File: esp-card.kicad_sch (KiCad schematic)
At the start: 15 parts, among them J1 Conn_01x01_Socket, J2 Conn_01x02_Socket, U1 XC6206P332MR, U2 ESP32-C3FH4, U3 TYPE_C-CQ-111PWB, U4 TS-1187A-B-A-B, U5 NH-B1010RGBT-HF, X1 CF4040M00015001

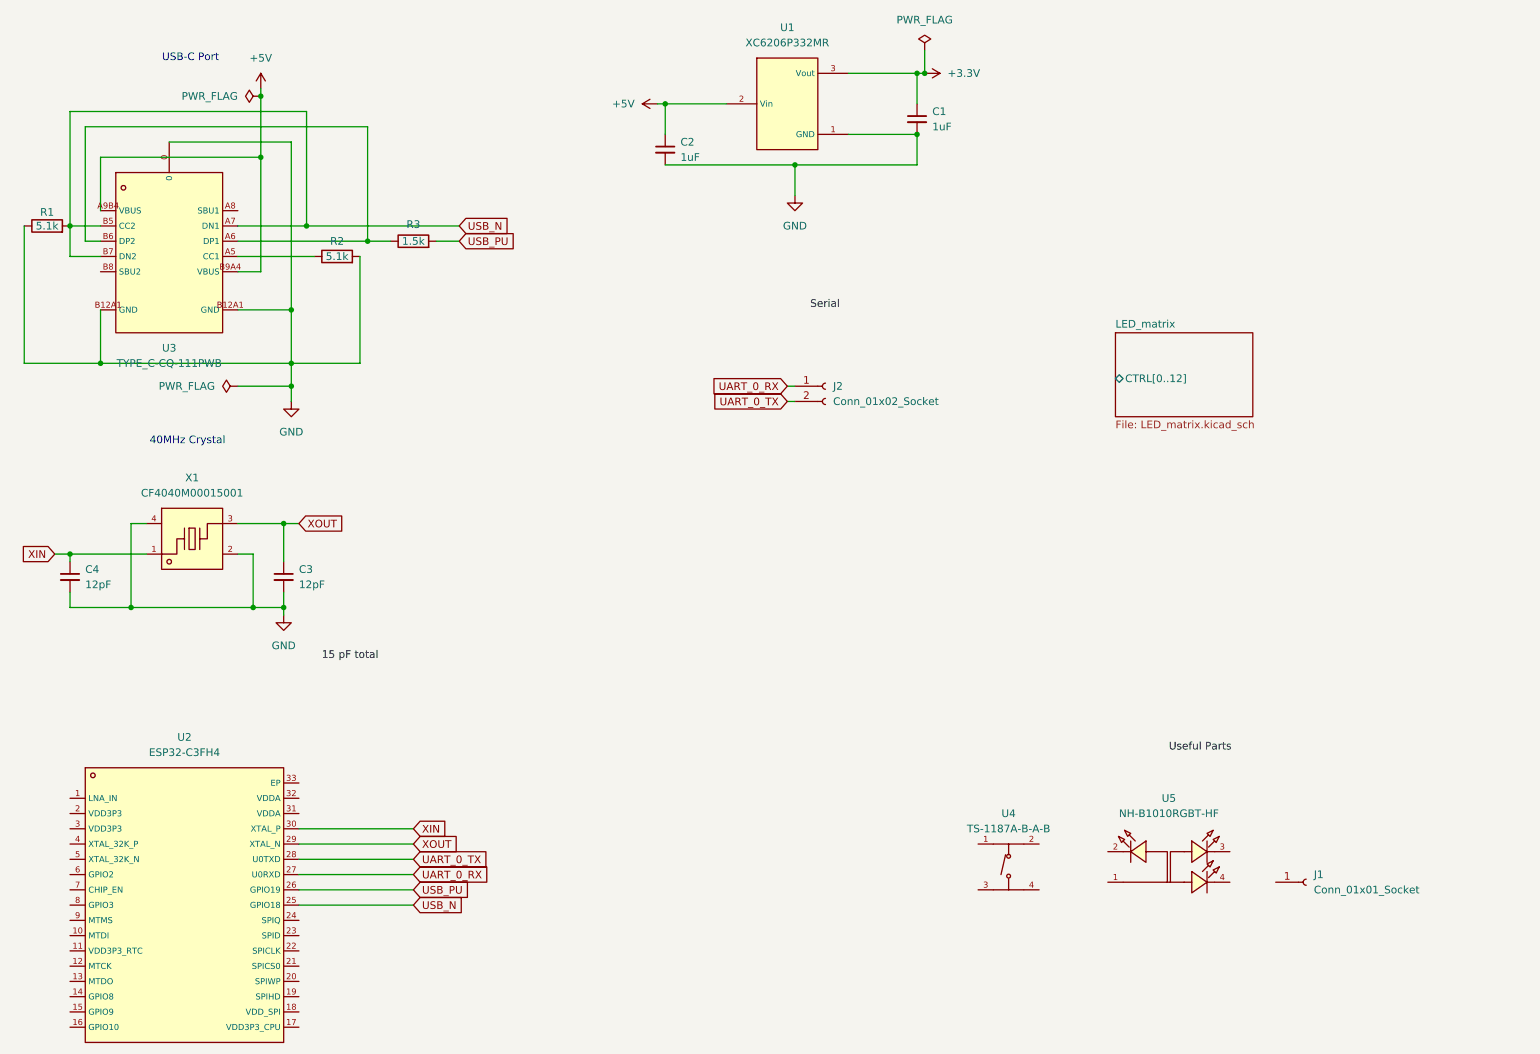
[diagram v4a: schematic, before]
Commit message: fix: corrected labels and hierarchy
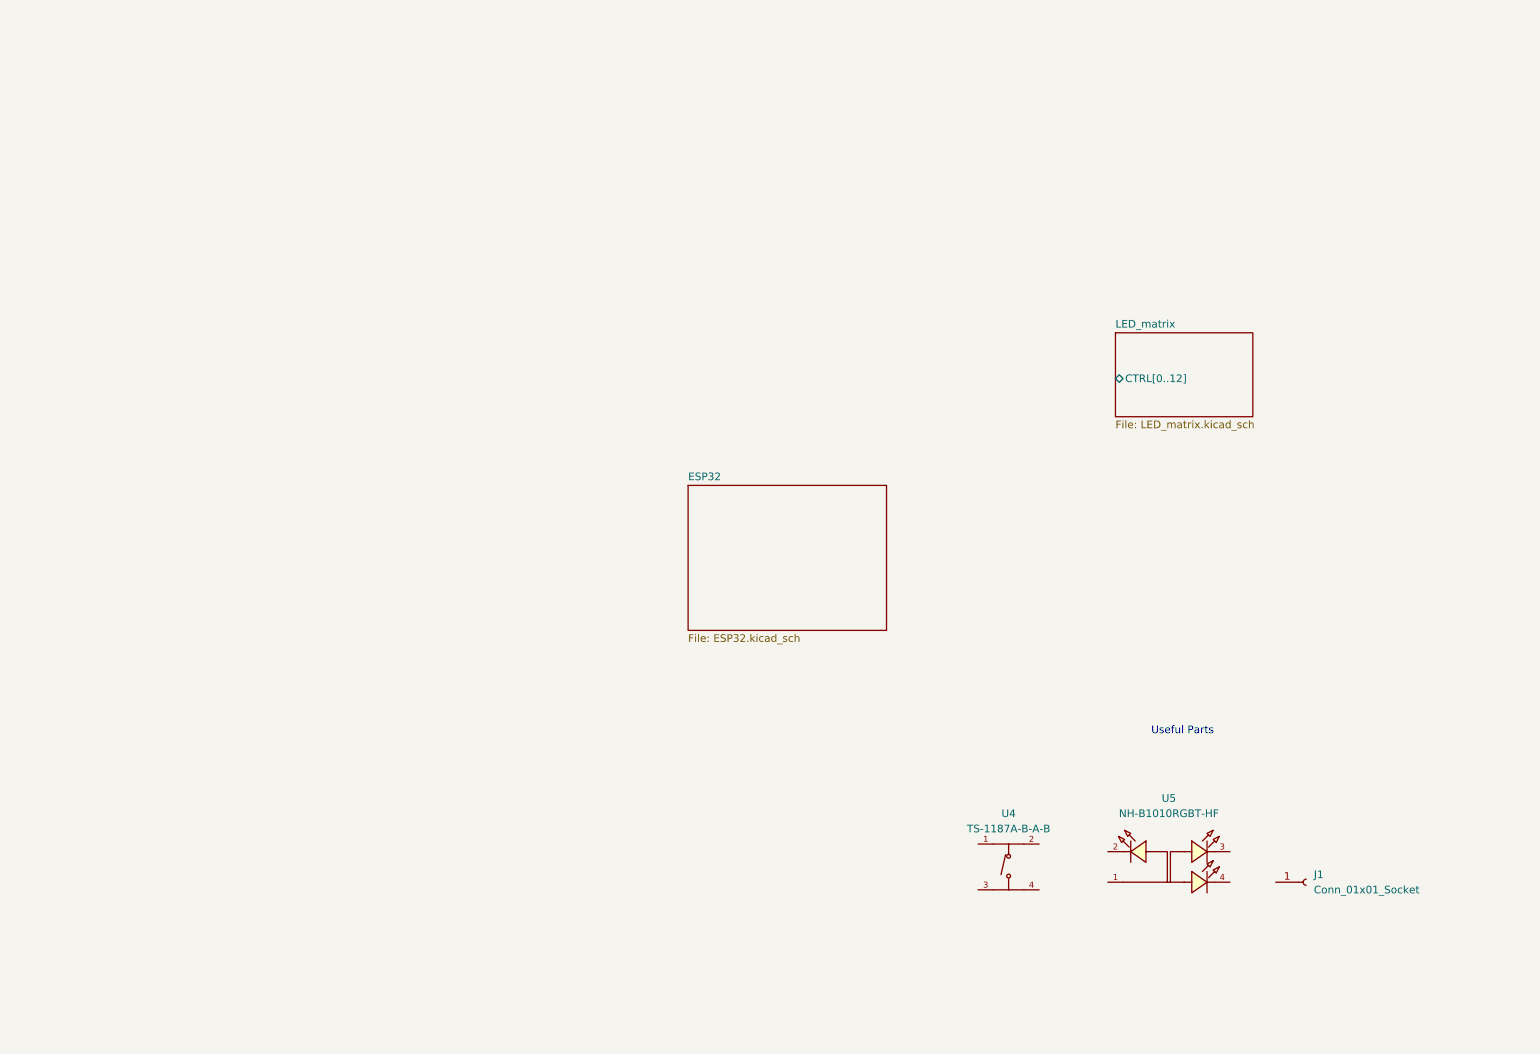
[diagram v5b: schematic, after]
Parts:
- removed C1, C2: 1uF, symbol Device:C_Small
- removed C3, C4: 12pF, symbol Device:C_Small
- removed J2: Conn_01x02_Socket, symbol Connector:Conn_01x02_Socket
- removed R1, R2: 5.1k, symbol Device:R
- removed R3: 1.5k, symbol Device:R
- removed U1: XC6206P332MR, footprint:SOT-23-3_L2.9-W1.6-P1.90-LS2.8-BR, symbol XC6206P332MR:XC6206P332MR
- removed U2: ESP32-C3FH4, footprint:QFN-32_L5.0-W5.0-P0.50-TL-EP3.7, symbol ESP32-C3FH4:ESP32-C3FH4
- removed U3: TYPE_C-CQ-111PWB, footprint:USB-C-SMD_HC-TYPE-C-16P-CB1.6, symbol TYPE_C-CQ-111PWB:TYPE_C-CQ-111PWB
- removed X1: CF4040M00015001, footprint:CRYSTAL-SMD_4P-L3.2-W2.5-BL_SIT8008BI, symbol CF4040M00015001:CF4040M00015001
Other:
- added sheet ESP32 (ESP32.kicad_sch)
- note added: "Useful Parts"
- note removed: "40MHz Crystal"
- note removed: "USB-C Port"

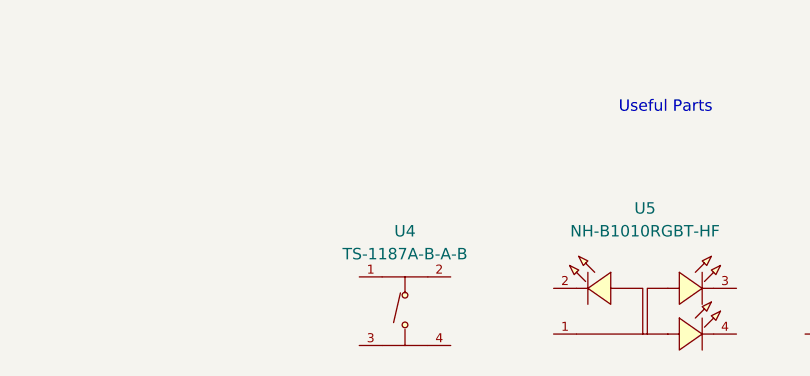
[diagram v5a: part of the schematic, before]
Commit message: Finish wiring up ESP basics
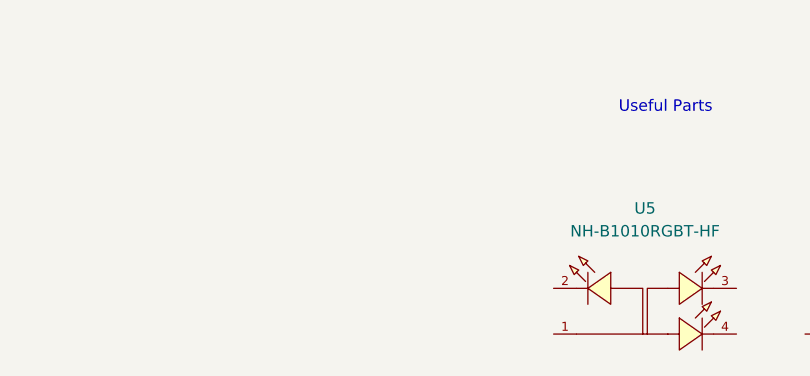
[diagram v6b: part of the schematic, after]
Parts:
- removed U4: TS-1187A-B-A-B, footprint:SW-SMD_4P-L5.1-W5.1-P3.70-LS6.5-TL-2, symbol TS-1187A-B-A-B:TS-1187A-B-A-B
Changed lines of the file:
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@@
-	)
-	(symbol
-		(lib_id "TS-1187A-B-A-B:TS-1187A-B-A-B")
-		(at 181.61 154.94 0)
-		(unit 1)
-		(exclude_from_sim no)
-		(in_bom yes)
-		(on_board yes)
-		(dnp no)
-		(fields_autoplaced yes)
-		(property "Reference" "U4"
-			(at 181.61 147.32 0)
-			(effects
-				(font
-					(size 1.27 1.27)
-				)
-			)
-		)
-		(property "Value" "TS-1187A-B-A-B"
-			(at 181.61 149.86 0)
-			(effects
-				(font
-					(size 1.27 1.27)
-				)
-			)
-		)
-		(property "Footprint" "footprint:SW-SMD_4P-L5.1-W5.1-P3.70-LS6.5-TL-2"
-			(at 181.61 165.1 0)
-			(effects
-				(font
-					(size 1.27 1.27)
-					(italic yes)
-				)
-				(hide yes)
-			)
-		)
-		(property "Datasheet" "https://item.szlcsc.com/300285.html"
-			(at 179.324 154.813 0)
-			(effects
-				(font
-					(size 1.27 1.27)
-				)
-				(justify left)
-				(hide yes)
-			)
-		)
-		(property "Description" ""
-			(at 181.61 154.94 0)
-			(effects
-				(font
-					(size 1.27 1.27)
-				)
-				(hide yes)
-			)
-		)
-		(property "LCSC" "C318884"
-			(at 181.61 154.94 0)
-			(effects
-				(font
-					(size 1.27 1.27)
-				)
-				(hide yes)
-			)
-		)
-		(pin "1"
-		)
-		(pin "4"
-		)
-		(pin "3"
-		)
-		(pin "2"
-		)
-		(instances
-			(project "esp-card"
-				(path "/93cf1a11-1660-4ae3-a523-02ca090cff0a"
-					(reference "U4")
-					(unit 1)
-				)
-			)
-		)
 	)
 	(symbol

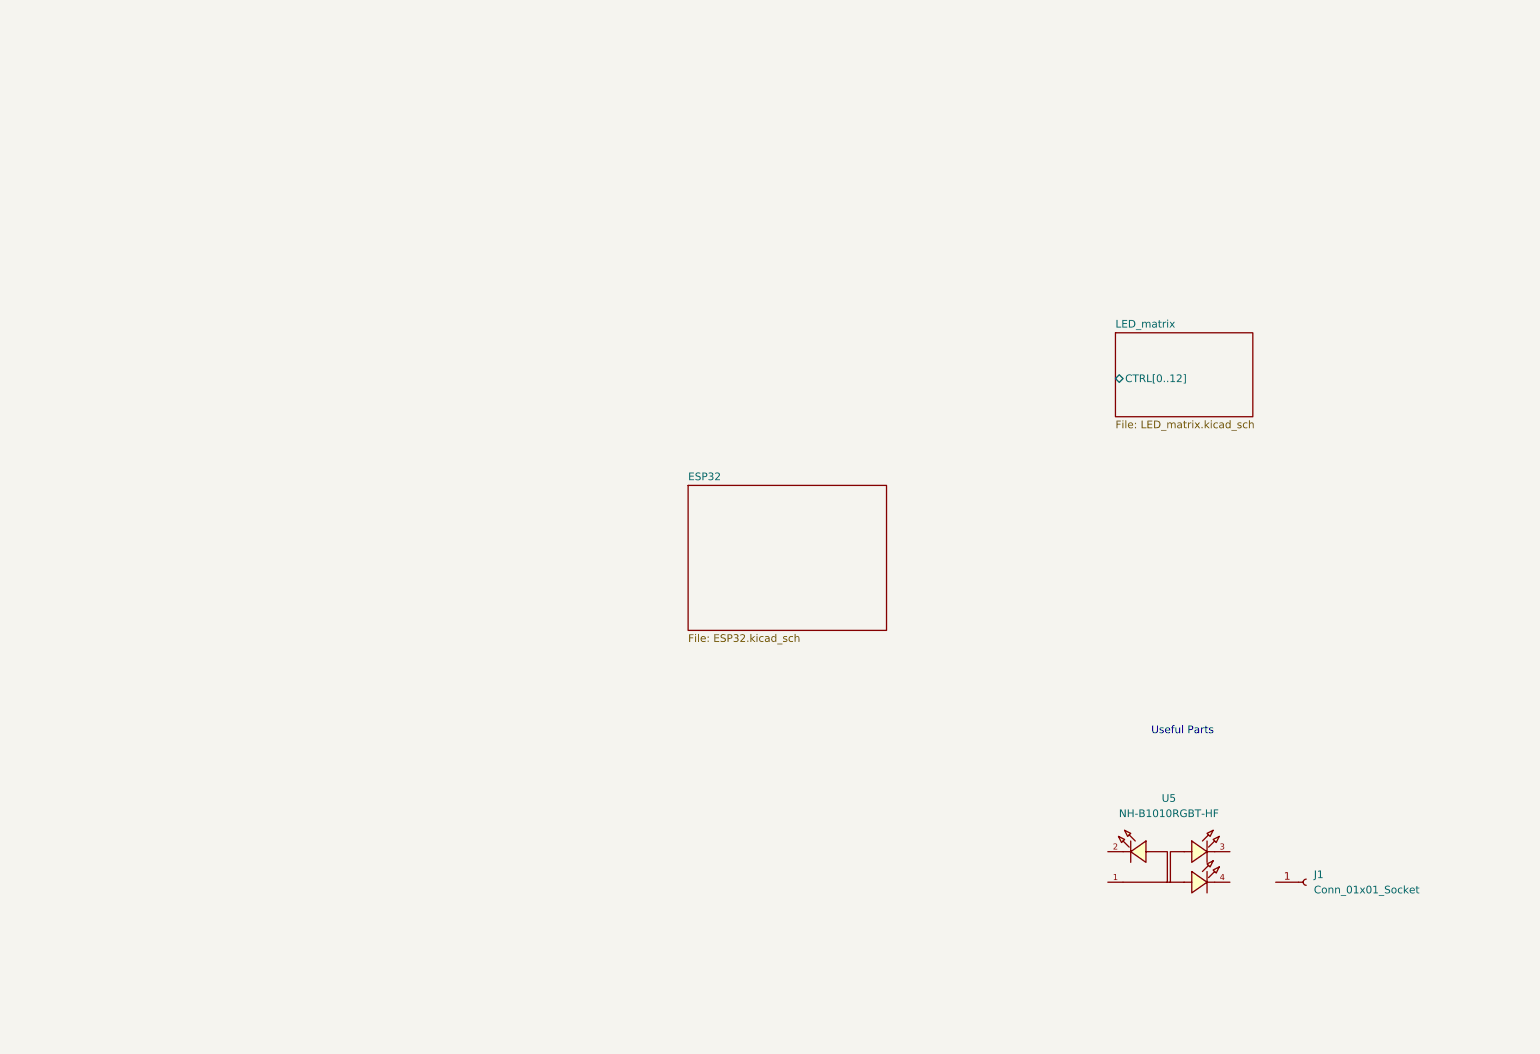
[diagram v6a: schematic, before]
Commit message: symbol fixes + placement
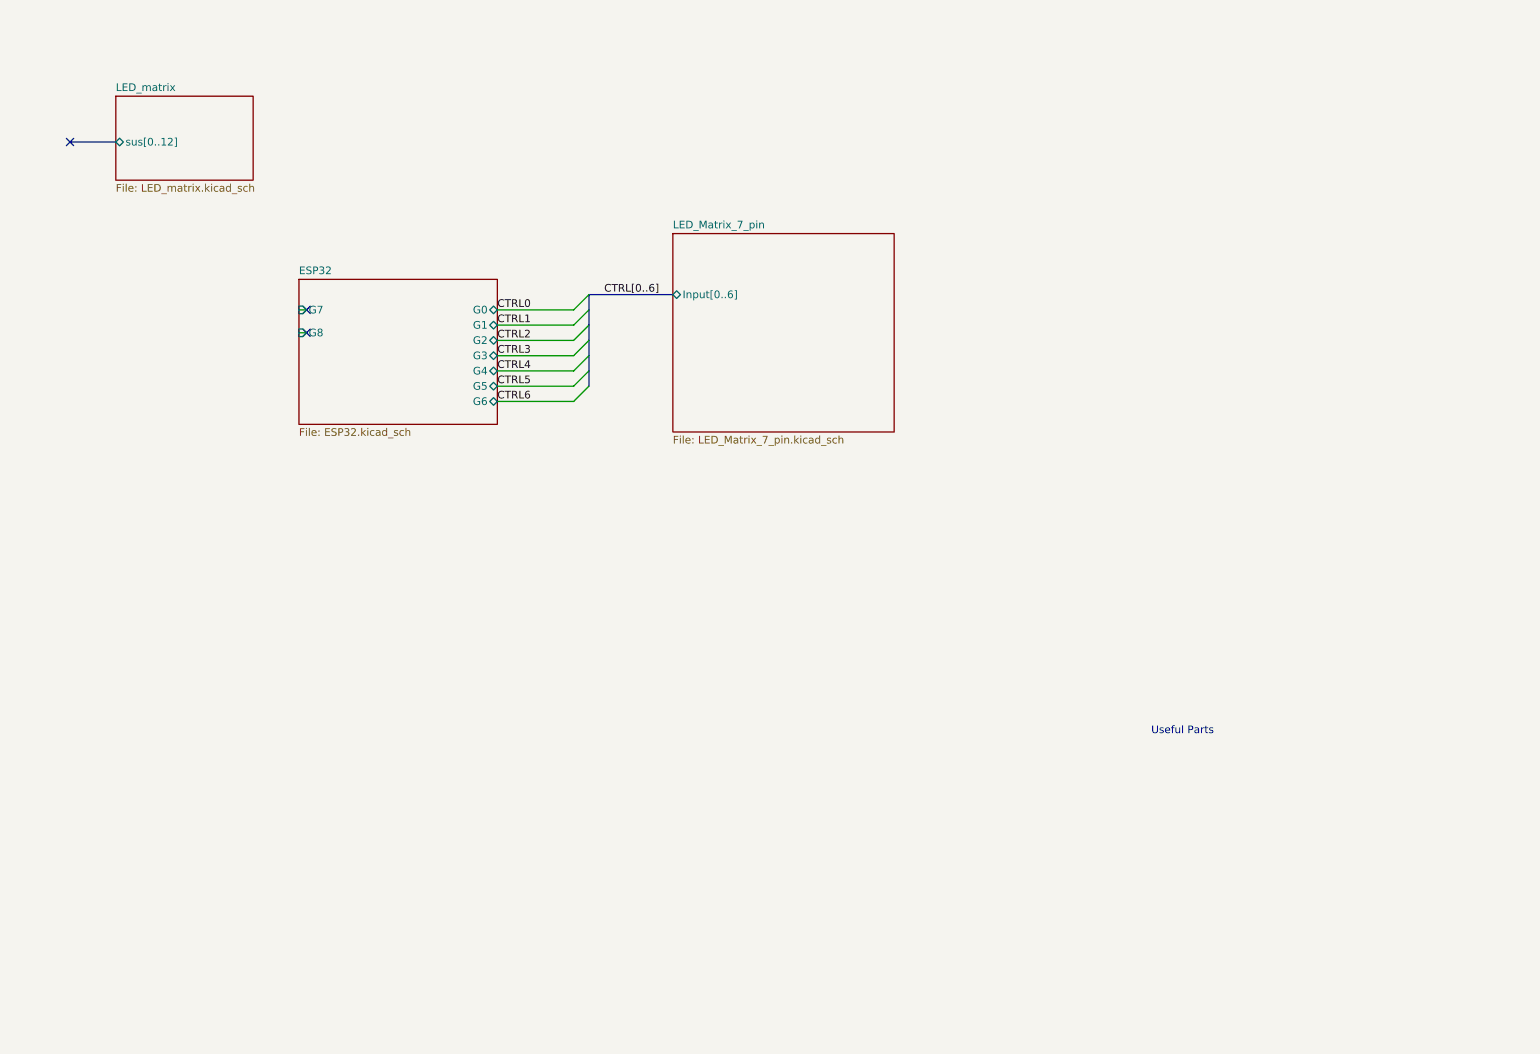
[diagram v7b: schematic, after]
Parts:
- removed J1: Conn_01x01_Socket, symbol Connector:Conn_01x01_Socket
- removed U5: NH-B1010RGBT-HF, footprint:LED-ARRAY-SMD_4P-L1.0-W1.0-TR_NH-B1010RGBT, symbol NH-B1010RGBT-HF:NH-B1010RGBT-HF
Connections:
- no-connect marks 0 -> 3
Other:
- added sheet LED_Matrix_7_pin (LED_Matrix_7_pin.kicad_sch)
- sheet ESP32 ports: added G0, G1, G2, G3, G4, G5, G6, G7, G8; removed none
- sheet LED_matrix ports: added sus[0..12]; removed CTRL[0..12]
